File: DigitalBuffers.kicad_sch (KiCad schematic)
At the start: 0 parts

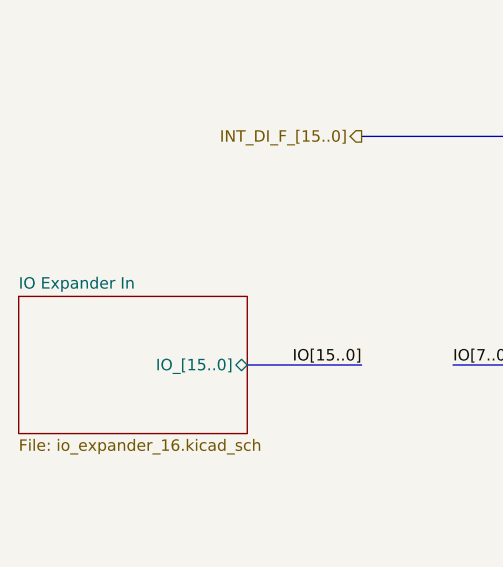
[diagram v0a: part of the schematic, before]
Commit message: analog inputs, timer IO
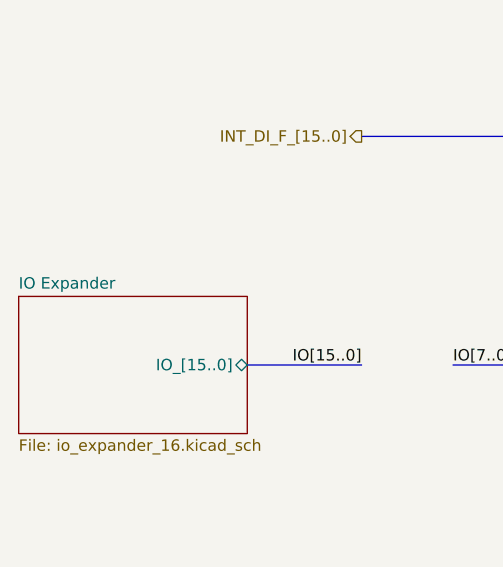
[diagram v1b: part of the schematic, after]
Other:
- sheet IO Expander In renamed IO Expander
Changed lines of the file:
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@@
     (stroke (width 0.1524) (type solid) (color 0 0 0 0))
     (fill (color 0 0 0 0.0000))
-    (property "Sheet name" "IO Expander In" (id 0) (at 50.8 72.9484 0)
+    (property "Sheet name" "IO Expander" (id 0) (at 50.8 72.9484 0)
       (effects (font (size 1.27 1.27)) (justify left bottom))
     )

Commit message: first draft schematic?
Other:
- sheet Digital In Slow ports: added VCC_OUT; removed none
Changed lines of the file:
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@@
+    (stroke (width 0) (type default) (color 0 0 0 0))
+  )
+  (wire (pts (xy 142.24 76.2) (xy 139.7 76.2))
     (stroke (width 0) (type default) (color 0 0 0 0))
   )
@@
   )
   (wire (pts (xy 139.7 111.76) (xy 149.86 111.76))
+    (stroke (width 0) (type default) (color 0 0 0 0))
+  )
+  (wire (pts (xy 142.24 73.66) (xy 142.24 76.2))
     (stroke (width 0) (type default) (color 0 0 0 0))
   )
@@
     )
     (property "Datasheet" "" (id 3) (at 142.24 48.26 0)
+      (effects (font (size 1.27 1.27)) hide)
+    )
+    (pin "1")
+  )
+  (symbol (lib_id "power:+12V") (at 142.24 73.66 0) (unit 1)
+    (in_bom yes) (on_board yes)
+    (property "Reference" "#PWR062" (id 0) (at 142.24 77.47 0)
+      (effects (font (size 1.27 1.27)) hide)
+    )
+    (property "Value" "+12V" (id 1) (at 142.24 70.104 0))
+    (property "Footprint" "" (id 2) (at 142.24 73.66 0)
+      (effects (font (size 1.27 1.27)) hide)
+    )
+    (property "Datasheet" "" (id 3) (at 142.24 73.66 0)
       (effects (font (size 1.27 1.27)) hide)
     )
@@
       (effects (font (size 1.27 1.27)) (justify left))
     )
-  )
+    (pin "VCC_OUT" passive (at 139.7 76.2 0)
+      (effects (font (size 1.27 1.27)) (justify right))
+    )
+  )
